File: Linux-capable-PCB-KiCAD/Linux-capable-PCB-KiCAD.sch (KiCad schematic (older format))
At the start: 31 parts

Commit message: od kuce
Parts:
- C? (x25): symbol device:C -> Linux-capable-PCB-KiCAD-rescue:C-device
- R? (x4): symbol device:R -> Linux-capable-PCB-KiCAD-rescue:R-device
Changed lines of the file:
@@
 $Descr A4 11693 8268
 encoding utf-8
-Sheet 1 2
+Sheet 1 3
 Title ""
 Date ""
@@
 $EndDescr
 $Comp
-L device:R R?
+L Linux-capable-PCB-KiCAD-rescue:R-device R?
 U 1 1 62A15ED1
 P 1850 2050
@@
 $EndComp
 $Comp
-L device:R R?
+L Linux-capable-PCB-KiCAD-rescue:R-device R?
 U 1 1 62A1672C
 P 1850 2450
@@
 $EndComp
 $Comp
-L device:C C?
+L Linux-capable-PCB-KiCAD-rescue:C-device C?
 U 1 1 62A16CCE
 P 1400 2050
@@
 $EndComp
 $Comp
-L device:C C?
+L Linux-capable-PCB-KiCAD-rescue:C-device C?
 U 1 1 62A17566
 P 1400 2450
@@
 	8850 4450 9100 4450
 $Comp
-L device:C C?
+L Linux-capable-PCB-KiCAD-rescue:C-device C?
 U 1 1 62AFB864
 P 8450 4350
@@
 Connection ~ 8500 1250
 $Comp
-L device:R R?
+L Linux-capable-PCB-KiCAD-rescue:R-device R?
 U 1 1 62D33586
 P 7300 2450
@@
 	6950 2450 7150 2450
 $Comp
-L device:C C?
+L Linux-capable-PCB-KiCAD-rescue:C-device C?
 U 1 1 62D5B2C7
 P 6950 1800
@@
 $EndComp
 $Comp
-L device:C C?
+L Linux-capable-PCB-KiCAD-rescue:C-device C?
 U 1 1 62D5B813
 P 7450 1800
@@
 HPVCCBP
 $Comp
-L device:C C?
+L Linux-capable-PCB-KiCAD-rescue:C-device C?
 U 1 1 62D90F5C
 P 6450 1800
@@
 $EndComp
 $Comp
-L device:C C?
+L Linux-capable-PCB-KiCAD-rescue:C-device C?
 U 1 1 62D91768
 P 6050 1800
@@
 $EndComp
 $Comp
-L device:C C?
+L Linux-capable-PCB-KiCAD-rescue:C-device C?
 U 1 1 62D91B4E
 P 5650 1800
@@
 $EndComp
 $Comp
-L device:C C?
+L Linux-capable-PCB-KiCAD-rescue:C-device C?
 U 1 1 62D91F34
 P 5200 1800
@@
 	5850 1400 6050 1400
 $Comp
-L device:C C?
+L Linux-capable-PCB-KiCAD-rescue:C-device C?
 U 1 1 62E138EE
 P 5650 2800
@@
 $EndComp
 $Comp
-L device:C C?
+L Linux-capable-PCB-KiCAD-rescue:C-device C?
 U 1 1 62E14225
 P 6050 2800
@@
 $EndComp
 $Comp
-L device:C C?
+L Linux-capable-PCB-KiCAD-rescue:C-device C?
 U 1 1 62E14403
 P 6450 2800
@@
 	6050 2550 6050 2600
 $Comp
-L device:C C?
+L Linux-capable-PCB-KiCAD-rescue:C-device C?
 U 1 1 62E86744
 P 5650 3900
@@
 $EndComp
 $Comp
-L device:C C?
+L Linux-capable-PCB-KiCAD-rescue:C-device C?
 U 1 1 62E86ADB
 P 6050 3900
@@
 	5850 3650 6050 3650
 $Comp
-L device:C C?
+L Linux-capable-PCB-KiCAD-rescue:C-device C?
 U 1 1 62ECBFC4
 P 6550 3900
@@
 $EndComp
 $Comp
-L device:C C?
+L Linux-capable-PCB-KiCAD-rescue:C-device C?
 U 1 1 62ECC222
 P 6950 3900
@@
 $EndComp
 $Comp
-L device:C C?
+L Linux-capable-PCB-KiCAD-rescue:C-device C?
 U 1 1 62ECC4B1
 P 7350 3900
@@
 $EndComp
 $Comp
-L device:C C?
+L Linux-capable-PCB-KiCAD-rescue:C-device C?
 U 1 1 62ECC791
 P 7700 3900
@@
 	7150 3650 7350 3650
 $Comp
-L device:C C?
+L Linux-capable-PCB-KiCAD-rescue:C-device C?
 U 1 1 62F64777
 P 5250 4900
@@
 $EndComp
 $Comp
-L device:C C?
+L Linux-capable-PCB-KiCAD-rescue:C-device C?
 U 1 1 62F64781
 P 5650 4900
@@
 $EndComp
 $Comp
-L device:C C?
+L Linux-capable-PCB-KiCAD-rescue:C-device C?
 U 1 1 62F6478B
 P 6050 4900
@@
 $EndComp
 $Comp
-L device:C C?
+L Linux-capable-PCB-KiCAD-rescue:C-device C?
 U 1 1 62FAB1B6
 P 6550 4950
@@
 $EndComp
 $Comp
-L device:C C?
+L Linux-capable-PCB-KiCAD-rescue:C-device C?
 U 1 1 62FAB1C0
 P 6950 4950
@@
 $EndComp
 $Comp
-L device:C C?
+L Linux-capable-PCB-KiCAD-rescue:C-device C?
 U 1 1 62FAB1CA
 P 7350 4950
@@
 $EndComp
 $Comp
-L device:C C?
+L Linux-capable-PCB-KiCAD-rescue:C-device C?
 U 1 1 62FAB1D4
 P 7700 4950
@@
 $EndSheet
 $Comp
-L device:R R?
+L Linux-capable-PCB-KiCAD-rescue:R-device R?
 U 1 1 62FC6A5E
 P 2250 5550

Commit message: RAM cip je spojen
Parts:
- added R? (x2): 22R, symbol Linux-capable-PCB-KiCAD-rescue:R-device
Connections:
- net labels added: adr[0..14], d[0..15], dba[0..2]
- net labels removed: address_bus[015], data_bus[0..15]
- wire segments 279 -> 328
- no-connect marks 0 -> 4

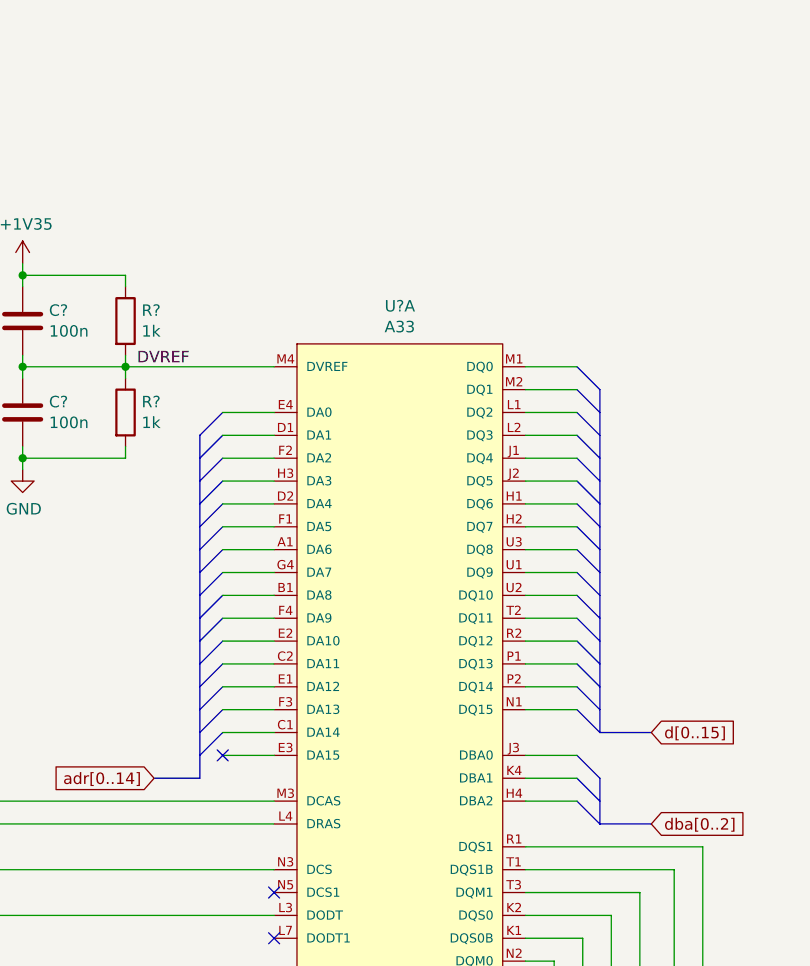
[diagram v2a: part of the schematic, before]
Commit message: added ESD protection, g sensor
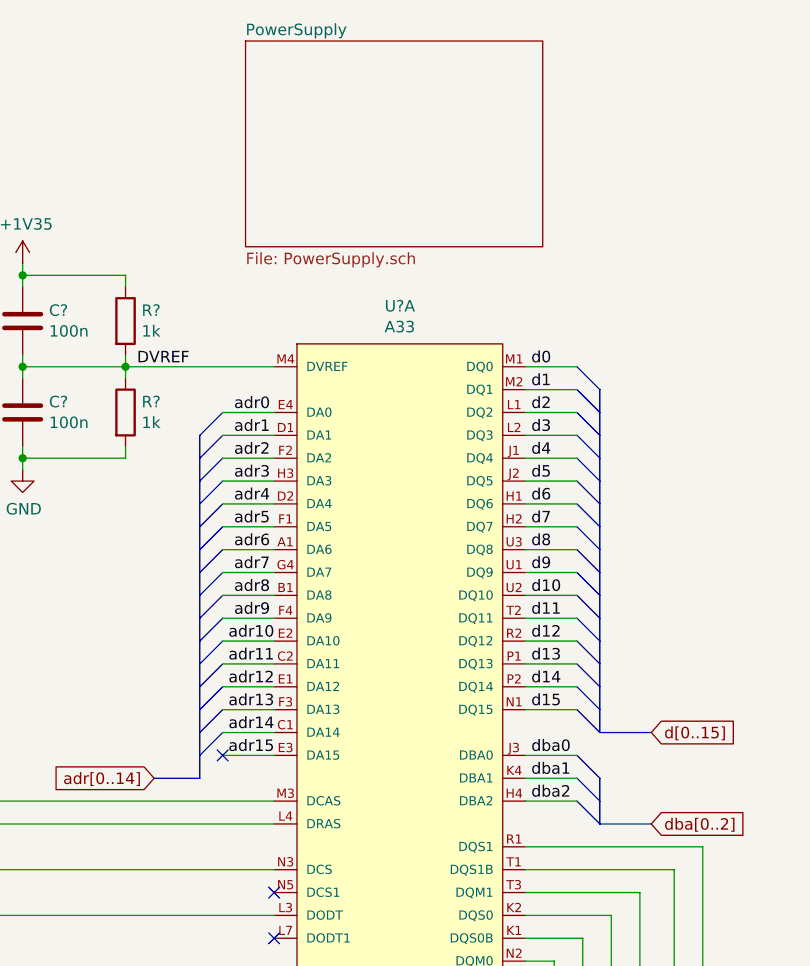
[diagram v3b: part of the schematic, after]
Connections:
- net labels added: adr0, adr1, adr10, adr11, adr12, adr13, adr14, adr15, adr2, adr3, adr4, adr5, adr6, adr7, adr8, adr9, d0, d1, d10, d11, d12, d13, d14, d15, d2, d3, d4, d5, d6, d7, d8, d9, dba0, dba1, dba2
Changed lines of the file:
@@
 $Descr A4 11693 8268
 encoding utf-8
-Sheet 1 4
+Sheet 1 5
 Title ""
 Date ""
@@
 Wire Bus Line
 	3925 2350 3925 3850
+Text Label 2325 2450 0    50   ~ 0
+adr0
+Text Label 2325 2550 0    50   ~ 0
+adr1
+Text Label 2325 2650 0    50   ~ 0
+adr2
+Text Label 2325 2750 0    50   ~ 0
+adr3
+Text Label 2325 2850 0    50   ~ 0
+adr4
+Text Label 2325 2950 0    50   ~ 0
+adr5
+Text Label 2325 3050 0    50   ~ 0
+adr6
+Text Label 2325 3150 0    50   ~ 0
+adr7
+Text Label 2325 3250 0    50   ~ 0
+adr8
+Text Label 2325 3350 0    50   ~ 0
+adr9
+Text Label 2300 3450 0    50   ~ 0
+adr10
+Text Label 2300 3550 0    50   ~ 0
+adr11
+Text Label 2300 3650 0    50   ~ 0
+adr12
+Text Label 2300 3750 0    50   ~ 0
+adr13
+Text Label 2300 3850 0    50   ~ 0
+adr14
+Text Label 2300 3950 0    50   ~ 0
+adr15
+Text Label 3625 2250 0    50   ~ 0
+d0
+Text Label 3625 2350 0    50   ~ 0
+d1
+Text Label 3625 2450 0    50   ~ 0
+d2
+Text Label 3625 2550 0    50   ~ 0
+d3
+Text Label 3625 2650 0    50   ~ 0
+d4
+Text Label 3625 2750 0    50   ~ 0
+d5
+Text Label 3625 2850 0    50   ~ 0
+d6
+Text Label 3625 2950 0    50   ~ 0
+d7
+Text Label 3625 3050 0    50   ~ 0
+d8
+Text Label 3625 3150 0    50   ~ 0
+d9
+Text Label 3625 3250 0    50   ~ 0
+d10
+Text Label 3625 3350 0    50   ~ 0
+d11
+Text Label 3625 3450 0    50   ~ 0
+d12
+Text Label 3625 3550 0    50   ~ 0
+d13
+Text Label 3625 3650 0    50   ~ 0
+d14
+Text Label 3625 3750 0    50   ~ 0
+d15
+Text Label 3625 3950 0    50   ~ 0
+dba0
+Text Label 3625 4050 0    50   ~ 0
+dba1
+Text Label 3625 4150 0    50   ~ 0
+dba2
+$Sheet
+S 2375 825  1300 900
+U 6385BAA8
+F0 "PowerSupply" 50
+F1 "PowerSupply.sch" 50
+$EndSheet
 $EndSCHEMATC

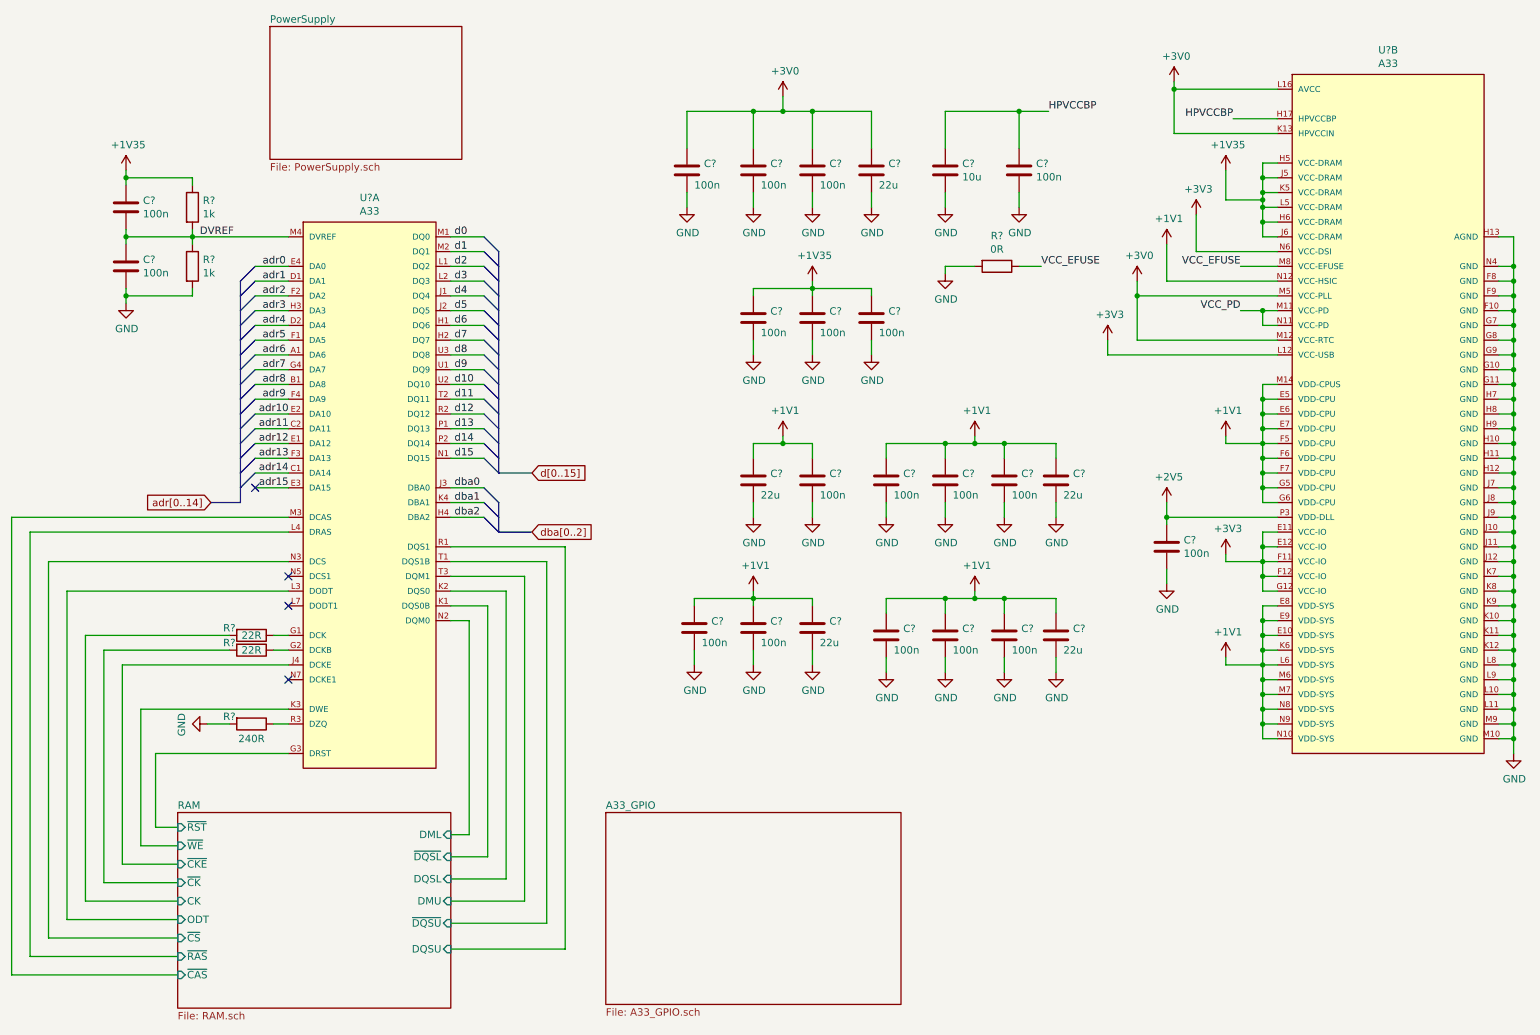
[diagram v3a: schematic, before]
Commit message: Power supply schematics
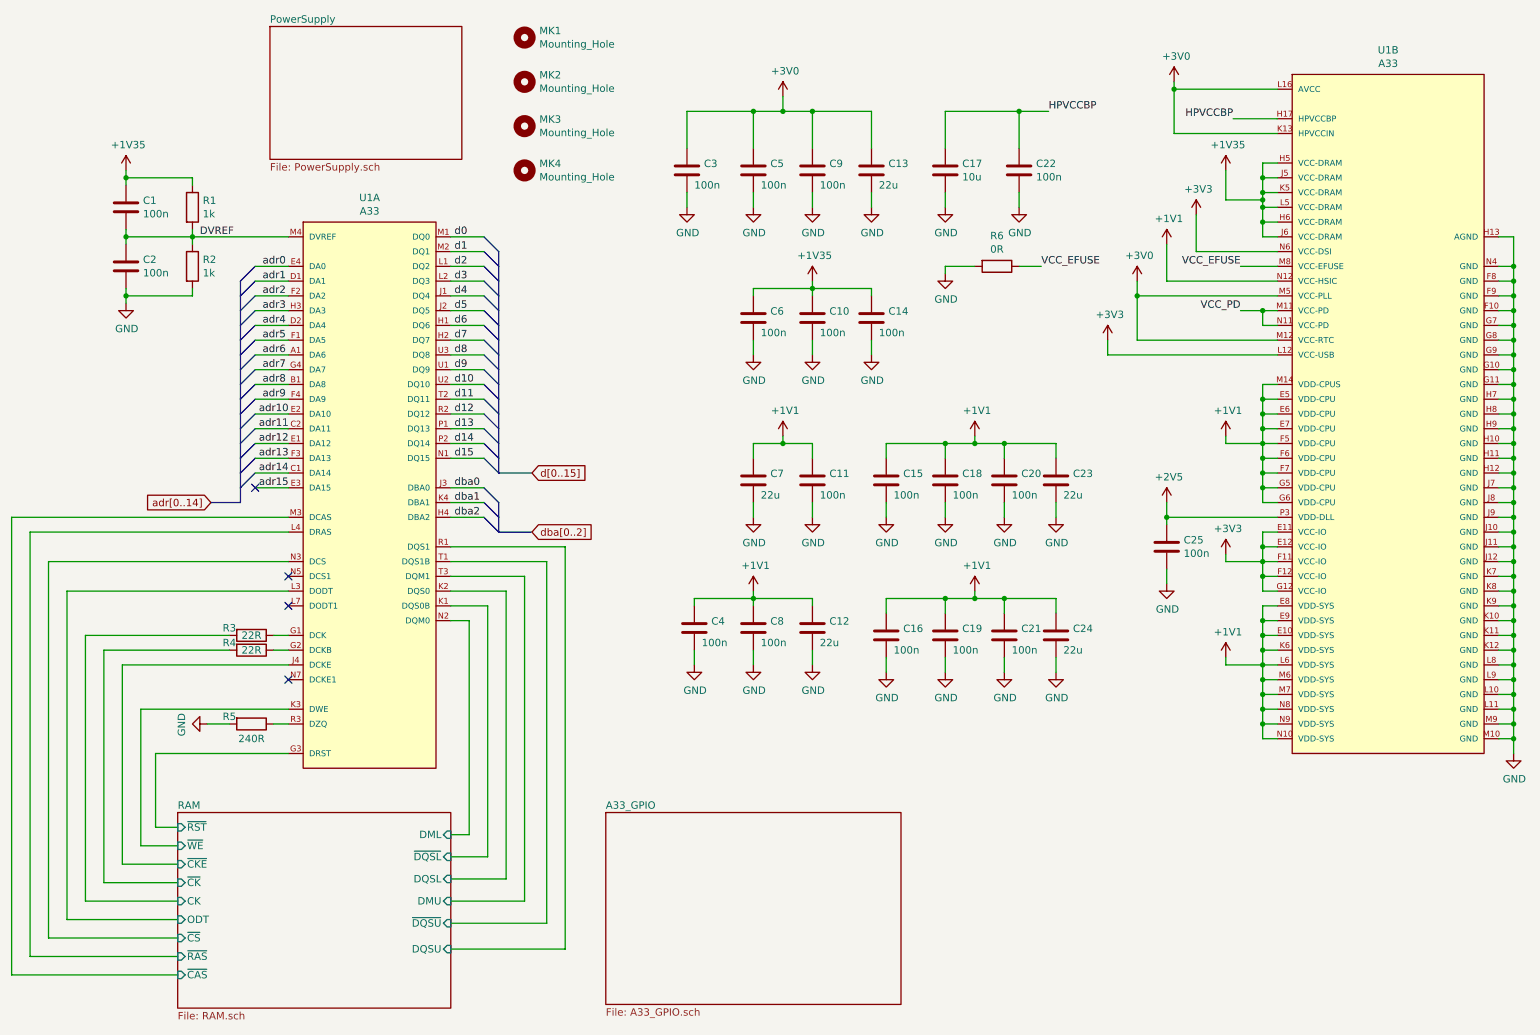
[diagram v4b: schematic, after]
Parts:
- added MK1, MK2, MK3, MK4: Mounting_Hole, symbol Mechanical:Mounting_Hole
- gave numbers to parts that had none: 32

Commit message: Added some footprints
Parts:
- U1: footprint Allwinner_Technology_Co.,_Ltd.-A33-* -> eec:Allwinner_Technology_Co.,_Ltd.-A33-0
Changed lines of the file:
@@
 F 0 "U1" H 9950 1515 50  0000 C CNN
 F 1 "A33" H 9950 1424 50  0000 C CNN
-F 2 "Allwinner_Technology_Co.,_Ltd.-A33-*" H 9100 1650 50  0001 L CNN
+F 2 "eec:Allwinner_Technology_Co.,_Ltd.-A33-0" H 9100 1650 50  0001 L CNN
 F 3 "http://dl.linux-sunxi.org/A33/A33_Datasheet_release1.0.pdf" H 9100 1750 50  0001 L CNN
 F 4 "1.8V ~ 3.3V" H 9100 1850 50  0001 L CNN "DC Supply Voltage for I/O"
@@
 F 0 "U1" H 3050 2515 50  0000 C CNN
 F 1 "A33" H 3050 2424 50  0000 C CNN
-F 2 "Allwinner_Technology_Co.,_Ltd.-A33-*" H 2400 2650 50  0001 L CNN
+F 2 "eec:Allwinner_Technology_Co.,_Ltd.-A33-0" H 2400 2650 50  0001 L CNN
 F 3 "http://dl.linux-sunxi.org/A33/A33_Datasheet_release1.0.pdf" H 2400 2750 50  0001 L CNN
 F 4 "1.8V ~ 3.3V" H 2400 2850 50  0001 L CNN "DC Supply Voltage for I/O"
@@
 F1 "PowerSupply.sch" 50
 $EndSheet
-Wire Bus Line
-	3925 4050 3925 4250
-Wire Bus Line
-	2175 2550 2175 4050
-Wire Bus Line
-	3925 2350 3925 3850
 $Comp
 L Mechanical:Mounting_Hole MK1
@@
 	1    0    0    -1
 $EndComp
+Wire Bus Line
+	3925 4050 3925 4250
+Wire Bus Line
+	2175 2550 2175 4050
+Wire Bus Line
+	3925 2350 3925 3850
 $EndSCHEMATC
